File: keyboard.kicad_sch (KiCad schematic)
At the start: 86 parts, among them J3 Conn_01x12_Pin, SW10 SW_SPST, SW11 SW_SPST, SW12 SW_SPST, SW13 SW_SPST, SW14 SW_SPST, SW15 SW_SPST, SW16 SW_SPST, SW17 SW_SPST, SW18 SW_SPST, SW19 SW_SPST, SW20 SW_SPST, SW21 SW_SPST, SW22 SW_SPST, SW23 SW_SPST, SW24 SW_SPST, SW25 SW_SPST, SW26 SW_SPST, SW27 SW_SPST, SW28 SW_SPST, SW29 SW_SPST, SW3 SW_SPST, SW30 SW_SPST, SW31 SW_SPST, SW32 SW_SPST, SW33 SW_SPST, SW34 SW_SPST, SW35 SW_SPST, SW36 SW_SPST, SW37 SW_SPST, SW38 SW_SPST, SW39 SW_SPST, SW4 SW_SPST, SW5 SW_SPST, SW6 SW_SPST, SW7 SW_SPST, SW8 SW_SPST, SW9 SW_SPST

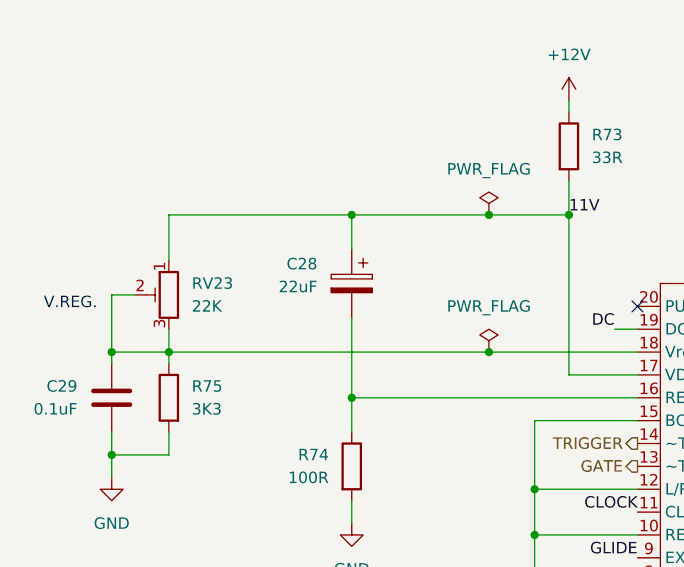
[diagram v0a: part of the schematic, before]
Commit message: Add missing values and connectors
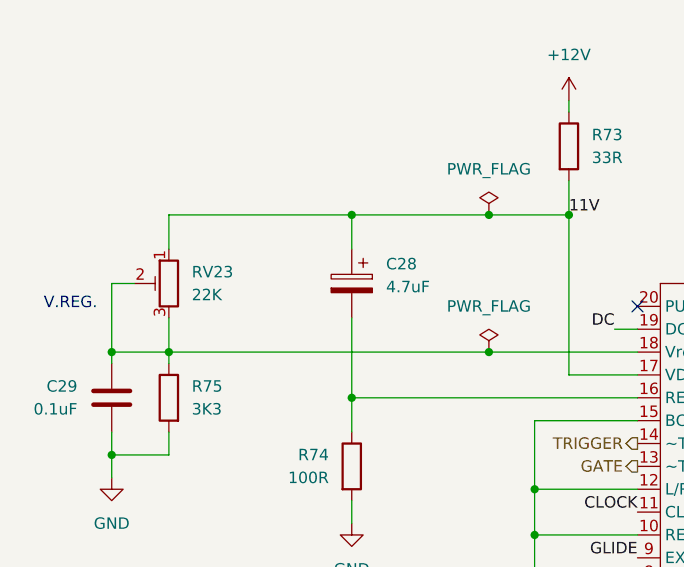
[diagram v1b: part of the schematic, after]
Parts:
- C28: value 22uF -> 4.7uF
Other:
- moved on the sheet: RV23
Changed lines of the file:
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@@
 	(wire
 		(pts
-			(xy 29.21 133.35) (xy 29.21 128.27)
+			(xy 29.21 132.08) (xy 29.21 128.27)
 		)
 		(stroke
@@
 	(wire
 		(pts
-			(xy 29.21 140.97) (xy 29.21 143.51)
+			(xy 29.21 139.7) (xy 29.21 143.51)
 		)
 		(stroke
@@
 	(wire
 		(pts
-			(xy 25.4 137.16) (xy 22.86 137.16)
+			(xy 25.4 135.89) (xy 22.86 135.89)
 		)
 		(stroke
@@
 	(wire
 		(pts
-			(xy 22.86 137.16) (xy 22.86 143.51)
+			(xy 22.86 135.89) (xy 22.86 143.51)
 		)
 		(stroke
@@
 	(symbol
 		(lib_id "Device:R_Potentiometer_Trim")
-		(at 29.21 137.16 0)
+		(at 29.21 135.89 0)
 		(mirror y)
 		(unit 1)
@@
 		(fields_autoplaced yes)
 		(property "Reference" "RV23"
-			(at 31.75 135.8899 0)
+			(at 31.75 134.6199 0)
 			(effects
 				(font
@@
 		)
 		(property "Value" "22K"
-			(at 31.75 138.4299 0)
+			(at 31.75 137.1599 0)
 			(effects
 				(font
@@
 		)
 		(property "Footprint" ""
-			(at 29.21 137.16 0)
+			(at 29.21 135.89 0)
 			(effects
 				(font
@@
 		)
 		(property "Datasheet" "~"
-			(at 29.21 137.16 0)
+			(at 29.21 135.89 0)
 			(effects
 				(font
@@
 		)
 		(property "Description" "Trim-potentiometer"
-			(at 29.21 137.16 0)
+			(at 29.21 135.89 0)
 			(effects
 				(font
@@
 		(fields_autoplaced yes)
 		(property "Reference" "C28"
-			(at 45.72 133.7309 0)
+			(at 53.34 133.7309 0)
 			(effects
 				(font
 					(size 1.27 1.27)
 				)
-				(justify left)
+				(justify right)
 			)
 		)
-		(property "Value" "22uF"
-			(at 45.72 136.2709 0)
+		(property "Value" "4.7uF"
+			(at 53.34 136.2709 0)
 			(effects
 				(font
 					(size 1.27 1.27)
 				)
-				(justify left)
+				(justify right)
 			)
 		)

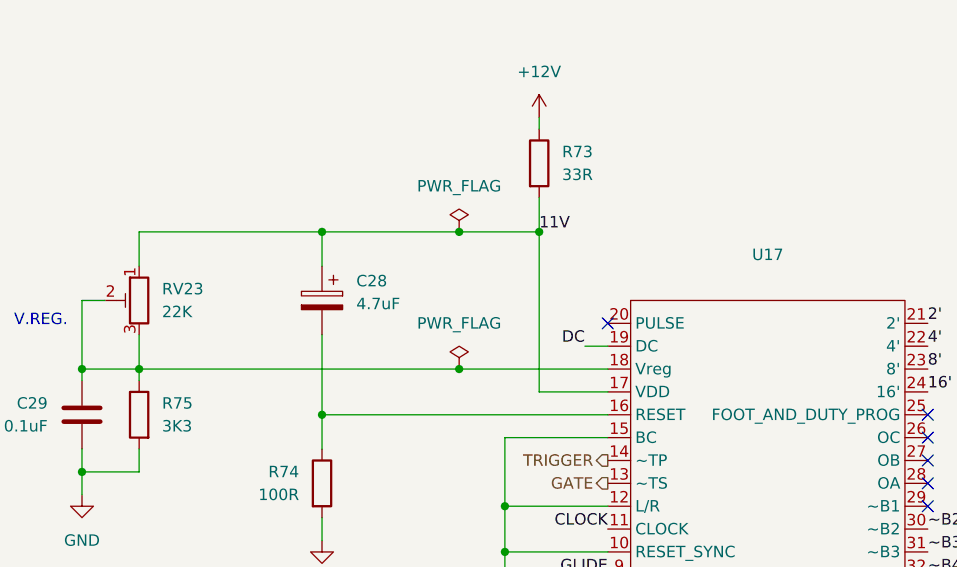
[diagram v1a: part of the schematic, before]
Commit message: Assign footprints and start PCB
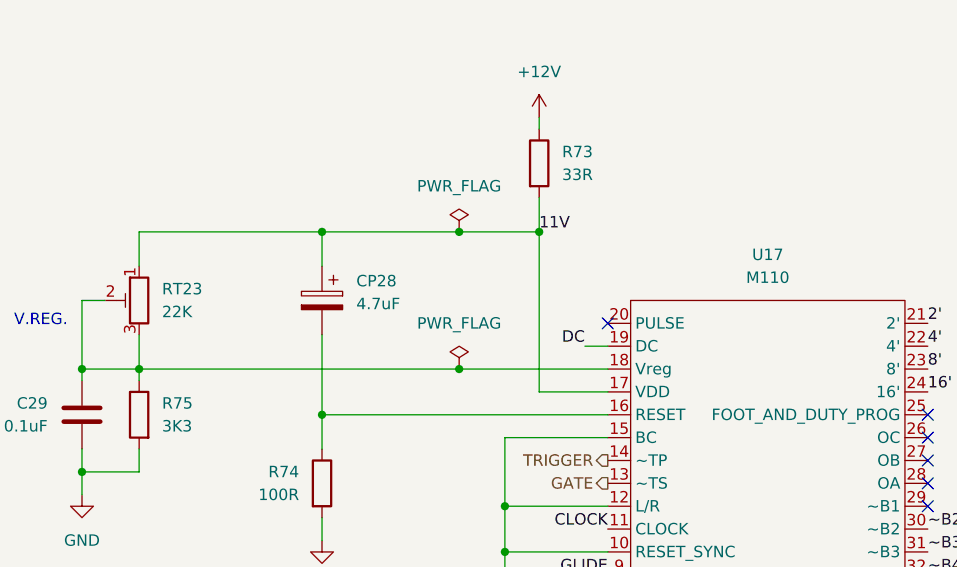
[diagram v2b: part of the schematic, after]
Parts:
- C29: footprint (none) -> Capacitor_THT:C_Disc_D5.0mm_W2.5mm_P5.00mm
- CP28: renamed from C28; footprint (none) -> Capacitor_THT:CP_Radial_D8.0mm_P3.80mm
- J3: footprint (none) -> Connector_PinHeader_2.54mm:PinHeader_1x12_P2.54mm_Vertical
- R106, R107, R108, R109, R73, R74, R75: footprint (none) -> Resistor_THT:R_Axial_DIN0204_L3.6mm_D1.6mm_P7.62mm_Horizontal
- RT23: renamed from RV23; footprint (none) -> Potentiometer_THT:Potentiometer_Bourns_3339P_Vertical_HandSoldering
- SW10, SW11, SW12, SW13, SW14, SW15, SW16, SW17, SW18, SW19, SW20, SW21, SW22, SW23, SW24, SW25, SW26, SW27, SW28, SW29, SW3, SW30, SW31, SW32, SW33, SW34, SW35, SW36, SW37, SW38, SW39, SW4, SW5, SW6, SW7, SW8, SW9: footprint (none) -> PCM_Jumper_AKL:Jumper_P30.48mm_D1.2mm
- U17: value ~ -> M110; footprint (none) -> Package_DIP:DIP-40_W15.24mm_LongPads
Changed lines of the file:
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@@
 			)
 		)
-		(property "Footprint" ""
+		(property "Footprint" "PCM_Jumper_AKL:Jumper_P30.48mm_D1.2mm"
 			(at 246.38 109.22 0)
 			(effects
@@
 			)
 		)
-		(property "Footprint" ""
+		(property "Footprint" "Resistor_THT:R_Axial_DIN0204_L3.6mm_D1.6mm_P7.62mm_Horizontal"
 			(at 47.752 156.21 90)
 			(effects
@@
 			)
 		)
-		(property "Footprint" ""
+		(property "Footprint" "Resistor_THT:R_Axial_DIN0204_L3.6mm_D1.6mm_P7.62mm_Horizontal"
 			(at 130.302 20.32 90)
 			(effects
@@
 			)
 		)
-		(property "Footprint" ""
+		(property "Footprint" "PCM_Jumper_AKL:Jumper_P30.48mm_D1.2mm"
 			(at 233.68 71.12 0)
 			(effects
@@
 			)
 		)
-		(property "Footprint" ""
+		(property "Footprint" "PCM_Jumper_AKL:Jumper_P30.48mm_D1.2mm"
 			(at 220.98 109.22 0)
 			(effects
@@
 			)
 		)
-		(property "Value" "~"
+		(property "Value" "M110"
 			(at 99.06 133.35 0)
 			(effects
@@
 			)
 		)
-		(property "Footprint" ""
+		(property "Footprint" "Package_DIP:DIP-40_W15.24mm_LongPads"
 			(at 81.28 186.69 0)
 			(effects
@@
 			)
 		)
-		(property "Footprint" ""
+		(property "Footprint" "PCM_Jumper_AKL:Jumper_P30.48mm_D1.2mm"
 			(at 259.08 71.12 0)
 			(effects
@@
 			)
 		)
-		(property "Footprint" ""
+		(property "Footprint" "PCM_Jumper_AKL:Jumper_P30.48mm_D1.2mm"
 			(at 259.08 109.22 0)
 			(effects
@@
 			)
 		)
-		(property "Footprint" ""
+		(property "Footprint" "PCM_Jumper_AKL:Jumper_P30.48mm_D1.2mm"
 			(at 195.58 109.22 0)
 			(effects
@@
 			)
 		)
-		(property "Footprint" ""
+		(property "Footprint" "PCM_Jumper_AKL:Jumper_P30.48mm_D1.2mm"
 			(at 170.18 109.22 0)
 			(effects
@@
 			)
 		)
-		(property "Footprint" ""
+		(property "Footprint" "Connector_PinHeader_2.54mm:PinHeader_1x12_P2.54mm_Vertical"
 			(at 22.86 36.83 0)
 			(effects
@@
 			)
 		)
-		(property "Footprint" ""
+		(property "Footprint" "Resistor_THT:R_Axial_DIN0204_L3.6mm_D1.6mm_P7.62mm_Horizontal"
 			(at 270.002 134.62 90)
 			(effects
@@
 			)
 		)
-		(property "Footprint" ""
+		(property "Footprint" "Resistor_THT:R_Axial_DIN0204_L3.6mm_D1.6mm_P7.62mm_Horizontal"
 			(at 130.302 58.42 90)
 			(effects
@@
 			)
 		)
-		(property "Footprint" ""
+		(property "Footprint" "Resistor_THT:R_Axial_DIN0204_L3.6mm_D1.6mm_P7.62mm_Horizontal"
 			(at 130.302 96.52 90)
 			(effects
@@
 		(on_board yes)
 		(dnp no)
-		(fields_autoplaced yes)
 		(property "Reference" "SW14"
 			(at 273.05 31.7499 90)
@@
 			)
 		)
-		(property "Footprint" ""
+		(property "Footprint" "PCM_Jumper_AKL:Jumper_P30.48mm_D1.2mm"
 			(at 271.78 33.02 0)
 			(effects
@@
 			)
 		)
-		(property "Footprint" ""
+		(property "Footprint" "PCM_Jumper_AKL:Jumper_P30.48mm_D1.2mm"
 			(at 233.68 109.22 0)
 			(effects
@@
 			)
 		)
-		(property "Footprint" ""
+		(property "Footprint" "PCM_Jumper_AKL:Jumper_P30.48mm_D1.2mm"
 			(at 271.78 147.32 0)
 			(effects
@@
 			)
 		)
-		(property "Footprint" ""
+		(property "Footprint" "PCM_Jumper_AKL:Jumper_P30.48mm_D1.2mm"
 			(at 182.88 109.22 0)
 			(effects
@@
 			)
 		)
-		(property "Footprint" ""
+		(property "Footprint" "Resistor_THT:R_Axial_DIN0204_L3.6mm_D1.6mm_P7.62mm_Horizontal"
 			(at 30.988 148.59 90)
 			(effects
@@
 			)
 		)
-		(property "Footprint" ""
+		(property "Footprint" "PCM_Jumper_AKL:Jumper_P30.48mm_D1.2mm"
 			(at 144.78 33.02 0)
 			(effects
@@
 			)
 		)
-		(property "Footprint" ""
+		(property "Footprint" "PCM_Jumper_AKL:Jumper_P30.48mm_D1.2mm"
 			(at 259.08 33.02 0)
 			(effects
@@
 			)
 		)
-		(property "Footprint" ""
+		(property "Footprint" "PCM_Jumper_AKL:Jumper_P30.48mm_D1.2mm"
 			(at 195.58 33.02 0)
 			(effects
@@
 			)
 		)
-		(property "Footprint" ""
+		(property "Footprint" "PCM_Jumper_AKL:Jumper_P30.48mm_D1.2mm"
 			(at 246.38 33.02 0)
 			(effects
@@
 			)
 		)
-		(property "Footprint" ""
+		(property "Footprint" "PCM_Jumper_AKL:Jumper_P30.48mm_D1.2mm"
 			(at 132.08 71.12 0)
 			(effects
@@
 			)
 		)
-		(property "Footprint" ""
+		(property "Footprint" "PCM_Jumper_AKL:Jumper_P30.48mm_D1.2mm"
 			(at 182.88 33.02 0)
 			(effects
@@
 			)
 		)
-		(property "Footprint" ""
+		(property "Footprint" "PCM_Jumper_AKL:Jumper_P30.48mm_D1.2mm"
 			(at 208.28 109.22 0)
 			(effects
@@
 			)
 		)
-		(property "Footprint" ""
+		(property "Footprint" "PCM_Jumper_AKL:Jumper_P30.48mm_D1.2mm"
 			(at 170.18 33.02 0)
 			(effects
@@
 		(dnp no)
 		(fields_autoplaced yes)
-		(property "Reference" "RV23"
+		(property "Reference" "RT23"
 			(at 31.75 134.6199 0)
 			(effects
@@
 			)
 		)
-		(property "Footprint" ""
+		(property "Footprint" "Potentiometer_THT:Potentiometer_Bourns_3339P_Vertical_HandSoldering"
 			(at 29.21 135.89 0)
 			(effects
@@
 			(project "jensx1000"
 				(path "/3c53febc-5769-4c45-8f8f-0aba2c04e944/53fd3068-c5f7-4c98-83e9-40af01ac41f9"
-					(reference "RV23")
+					(reference "RT23")
 					(unit 1)
 				)
@@
 			)
 		)
-		(property "Footprint" ""
+		(property "Footprint" "PCM_Jumper_AKL:Jumper_P30.48mm_D1.2mm"
 			(at 157.48 109.22 0)
 			(effects
@@
 			)
 		)
-		(property "Footprint" ""
+		(property "Footprint" "PCM_Jumper_AKL:Jumper_P30.48mm_D1.2mm"
 			(at 208.28 71.12 0)
 			(effects
@@
 			)
 		)
-		(property "Footprint" ""
+		(property "Footprint" "PCM_Jumper_AKL:Jumper_P30.48mm_D1.2mm"
 			(at 271.78 109.22 0)
 			(effects
@@
 			)
 		)
-		(property "Footprint" ""
+		(property "Footprint" "PCM_Jumper_AKL:Jumper_P30.48mm_D1.2mm"
 			(at 208.28 33.02 0)
 			(effects
@@
 			)
 		)
-		(property "Footprint" ""
+		(property "Footprint" "PCM_Jumper_AKL:Jumper_P30.48mm_D1.2mm"
 			(at 157.48 33.02 0)
 			(effects
@@
 			)
 		)
-		(property "Footprint" ""
+		(property "Footprint" "Capacitor_THT:C_Disc_D5.0mm_W2.5mm_P5.00mm"
 			(at 23.8252 152.4 0)
 			(effects
@@
 			)
 		)
-		(property "Footprint" ""
+		(property "Footprint" "PCM_Jumper_AKL:Jumper_P30.48mm_D1.2mm"
 			(at 132.08 109.22 0)
 			(effects
@@
 			)
 		)
-		(property "Footprint" ""
+		(property "Footprint" "PCM_Jumper_AKL:Jumper_P30.48mm_D1.2mm"
 			(at 144.78 71.12 0)
 			(effects
@@
 		(dnp no)
 		(fields_autoplaced yes)
-		(property "Reference" "C28"
+		(property "Reference" "CP28"
 			(at 53.34 133.7309 0)
 			(effects
@@
 			)
 		)
-		(property "Footprint" ""
+		(property "Footprint" "Capacitor_THT:CP_Radial_D8.0mm_P3.80mm"
 			(at 48.5648 139.7 0)
 			(effects
@@
 			(project "jensx1000"
 				(path "/3c53febc-5769-4c45-8f8f-0aba2c04e944/53fd3068-c5f7-4c98-83e9-40af01ac41f9"
-					(reference "C28")
+					(reference "CP28")
 					(unit 1)
 				)
@@
 			)
 		)
-		(property "Footprint" ""
+		(property "Footprint" "PCM_Jumper_AKL:Jumper_P30.48mm_D1.2mm"
 			(at 132.08 33.02 0)
 			(effects
@@
 			)
 		)
-		(property "Footprint" ""
+		(property "Footprint" "PCM_Jumper_AKL:Jumper_P30.48mm_D1.2mm"
 			(at 170.18 71.12 0)
 			(effects
@@
 			)
 		)
-		(property "Footprint" ""
+		(property "Footprint" "PCM_Jumper_AKL:Jumper_P30.48mm_D1.2mm"
 			(at 246.38 71.12 0)
 			(effects
@@
 			)
 		)
-		(property "Footprint" ""
+		(property "Footprint" "PCM_Jumper_AKL:Jumper_P30.48mm_D1.2mm"
 			(at 195.58 71.12 0)
 			(effects
@@
 			)
 		)
-		(property "Footprint" ""
+		(property "Footprint" "Resistor_THT:R_Axial_DIN0204_L3.6mm_D1.6mm_P7.62mm_Horizontal"
 			(at 71.882 120.65 90)
 			(effects
@@
 			)
 		)
-		(property "Footprint" ""
+		(property "Footprint" "PCM_Jumper_AKL:Jumper_P30.48mm_D1.2mm"
 			(at 220.98 33.02 0)
 			(effects
@@
 			)
 		)
-		(property "Footprint" ""
+		(property "Footprint" "PCM_Jumper_AKL:Jumper_P30.48mm_D1.2mm"
 			(at 157.48 71.12 0)
 			(effects
@@
 			)
 		)
-		(property "Footprint" ""
+		(property "Footprint" "PCM_Jumper_AKL:Jumper_P30.48mm_D1.2mm"
 			(at 233.68 33.02 0)
 			(effects
@@
 			)
 		)
-		(property "Footprint" ""
+		(property "Footprint" "PCM_Jumper_AKL:Jumper_P30.48mm_D1.2mm"
 			(at 182.88 71.12 0)
 			(effects
@@
 			)
 		)
-		(property "Footprint" ""
+		(property "Footprint" "PCM_Jumper_AKL:Jumper_P30.48mm_D1.2mm"
 			(at 271.78 71.12 0)
 			(effects
@@
 			)
 		)
-		(property "Footprint" ""
+		(property "Footprint" "PCM_Jumper_AKL:Jumper_P30.48mm_D1.2mm"
 			(at 144.78 109.22 0)
 			(effects
@@
 			)
 		)
-		(property "Footprint" ""
+		(property "Footprint" "PCM_Jumper_AKL:Jumper_P30.48mm_D1.2mm"
 			(at 220.98 71.12 0)
 			(effects

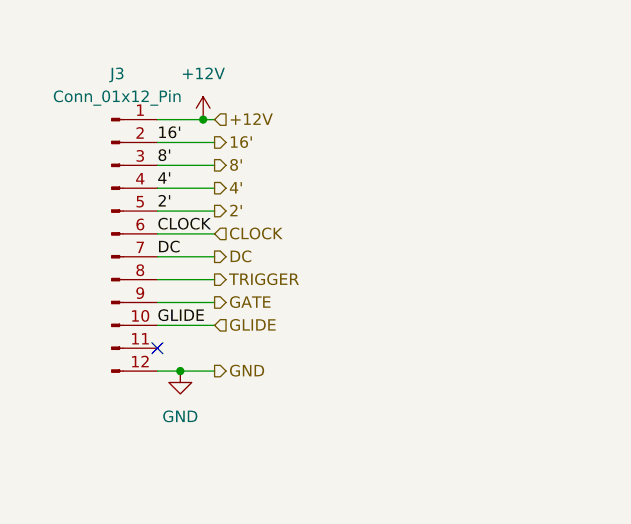
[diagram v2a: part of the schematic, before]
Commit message: Added layout photos, noise & ADSR components are in position
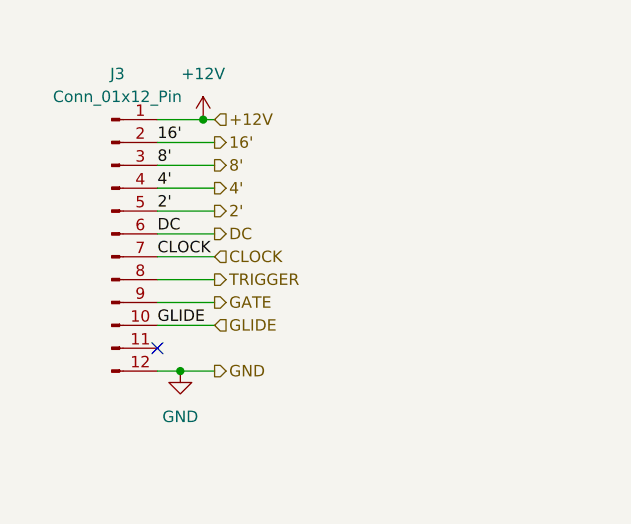
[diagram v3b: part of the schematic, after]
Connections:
- net CLOCK: now also J3.7 (Pin_7); no longer J3.6 (Pin_6)
- net DC: now also J3.6 (Pin_6); no longer J3.7 (Pin_7)
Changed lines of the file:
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@@
+	(wire
+		(pts
+			(xy 27.94 36.83) (xy 34.29 36.83)
+		)
+		(stroke
+			(width 0)
+			(type default)
+		)
+	)
 	(wire
 		(pts
 			(xy 27.94 39.37) (xy 34.29 39.37)
-		)
-		(stroke
-			(width 0)
-			(type default)
-		)
-	)
-	(wire
-		(pts
-			(xy 27.94 36.83) (xy 34.29 36.83)
 		)
 		(stroke
@@
 	)
 	(label "CLOCK"
-		(at 27.94 36.83 0)
+		(at 27.94 39.37 0)
 		(effects
 			(font
@@
 	)
 	(label "DC"
-		(at 27.94 39.37 0)
+		(at 27.94 36.83 0)
 		(effects
 			(font
@@
 	(hierarchical_label "DC"
 		(shape output)
-		(at 34.29 39.37 0)
+		(at 34.29 36.83 0)
 		(effects
 			(font
@@
 	(hierarchical_label "CLOCK"
 		(shape input)
-		(at 34.29 36.83 0)
-		(effects
-			(font
+		(at 34.29 39.37 0)
+		(effects
+			(font
